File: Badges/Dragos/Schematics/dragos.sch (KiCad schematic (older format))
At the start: 31 parts, among them J1 Conn_01x02, J2 Left, J3 Right, J4 Conn_01x02, J5 Prog, J7 USB_C_Receptacle, SW1 SW_DIP_x01, SW2 Prog, SW3 Power, U1 STM32F042F6Px, U2 TLV1117-33, U3 HX4056, Y1 8MHz

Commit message: Progress on Dragos badge
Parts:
- removed J1, J4: Conn_01x02, Connector_PinHeader_2.54mm:PinHeader_1x02_P2.54mm_Vertical, symbol badge-rescue:Conn_01x02
- removed J2: Left, Connector_PinHeader_2.54mm:PinHeader_1x05_P2.54mm_Vertical, symbol Connector_Generic:Conn_01x05
- removed J3: Right, Connector_PinHeader_2.54mm:PinHeader_1x06_P2.54mm_Vertical, symbol Connector_Generic:Conn_01x06
- removed J5: Prog, Connector_PinHeader_2.54mm:PinHeader_1x04_P2.54mm_Vertical, symbol badge-rescue:Conn_01x04
- removed R4: 0ohm, Resistors_SMD:R_0805_HandSoldering, symbol badge-rescue:R
- removed SW2: Prog, BreadBoardPwr:SK-3296S_switch, symbol Switch:SW_SPDT
- removed U1: STM32F042F6Px, Package_SO:TSSOP-20_4.4x6.5mm_P0.65mm, symbol MCU_ST_STM32F0:STM32F042F6Px
- removed Y1: 8MHz, Crystal:Crystal_SMD_5032-2Pin_5.0x3.2mm, symbol Device:Crystal_Small
- added C12: 100nF, Capacitor_SMD:C_0805_2012Metric, symbol Device:C_Small
- added C13: 1uF, Capacitor_SMD:C_0805_2012Metric, symbol Device:C_Small
- added C14: 4.7uF, Capacitor_SMD:C_0805_2012Metric, symbol Device:C_Small
- added C15, C16: 10pF, Capacitor_SMD:C_0805_2012Metric, symbol Device:C_Small
- added C17, C18: 2.2pF, Capacitor_SMD:C_0805_2012Metric, symbol Device:C_Small
- added D1, D2: LED, LED_SMD:LED_0603_1608Metric, symbol Device:LED
- added D3: LED_ALT, symbol Device:LED_ALT
- added J1: One, Connector_PinHeader_2.54mm:PinHeader_1x08_P2.54mm_Vertical, symbol Connector_Generic:Conn_01x08
- added J2: Two, Connector_PinHeader_2.54mm:PinHeader_1x11_P2.54mm_Vertical, symbol Connector_Generic:Conn_01x11
- added J3: CC2530-ISP, Connector_PinHeader_2.54mm:PinHeader_2x05_P2.54mm_Vertical, symbol Connector_Generic:Conn_02x05_Odd_Even
- added J4: Three, Connector_PinHeader_2.54mm:PinHeader_1x14_P2.54mm_Vertical, symbol Connector_Generic:Conn_01x14
- added J5: Prog, Connector_PinHeader_2.54mm:PinHeader_1x06_P2.54mm_Vertical, symbol Connector_Generic:Conn_01x06
- added J6: Oled_FFS, Connector_FFC-FPC:TE_1-84953-0_1x10-1MP_P1.0mm_Horizontal, symbol Connector_Generic:Conn_01x11
- added J8: Four, Connector_PinHeader_2.54mm:PinHeader_1x13_P2.54mm_Vertical, symbol Connector_Generic:Conn_01x13
- added J9: BreadboardPwr, Connector_PinHeader_2.54mm:PinHeader_1x02_P2.54mm_Vertical, symbol Connector_Generic:Conn_01x02
- added L1: L_Small, Inductor_SMD:L_0603_1608Metric, symbol Device:L_Small
- added R10, R13, R14, R4, R7, R8: 4k7, Resistor_SMD:R_0805_2012Metric, symbol Device:R_Small
- added R11, R12: 330Ohm, Resistor_SMD:R_0805_2012Metric, symbol Device:R_Small
- added R9: 1k, Resistor_SMD:R_0805_2012Metric, symbol Device:R_Small
- added SW2, SW4: SW_DIP_x01, Dragos:1TS002E-2500-2500-CT-HYP-Button, symbol Switch:SW_DIP_x01
- added U1: STM32F411RETx, Package_QFP:LQFP-64_10x10mm_P0.5mm, symbol MCU_ST_STM32F4:STM32F411RETx
- added U4: EByte-CC2530, RF_Module:E18-MS1-PCB, symbol Dragos:EByte-CC2530
- added U5: K1-5202UA-03(5Way_Switch), Dragos:K1-5202UA-03(5way-switch), symbol Dragos:K1-5202UA-03(5Way_Switch)
- added Y1: 12MHz, Crystal:Crystal_SMD_SeikoEpson_TSX3225-4Pin_3.2x2.5mm, symbol Device:Crystal_GND24
- added Y2: 32.768kHz, Crystal:Crystal_SMD_3215-2Pin_3.2x1.5mm, symbol Device:Crystal_Small
- C1, C2: value 20pF -> 100nF
- C4: value 4.7uF -> 100nF
- C6: value 1uF -> 4.7uF
- C7: value 10nF -> 100nF
- R3: value 10k -> 100k
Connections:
- net labels added: Boot0, PA11, PA12, PA13, PA14, PA15, PA8, PB0, PB10, PB12, PB13, PB14, PB15, PB2, PB3, PB4, PB5, PB6, PB7, PB8, PB9, PC0, PC1, PC10, PC11, PC12, PC13, PC2, PC3, PC4, PC5, PC6, PC7, PC8, PC9, PD2
- net labels removed: BOOT0, PF0, PF1, Stat1, Stat2
- wire segments 73 -> 152
- no-connect marks 11 -> 32
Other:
- note added: "Battery Charger IC\n"
- note added: "Boot1"
- note added: "Eye Light, Reverse mount LED"
- note added: "Filter Caps\n"
- note added: "I2C Pullups"
- note added: "Voltage Regulation"
- moved on the sheet: BT1, C10, C11, C8, C9, J7, R1, R2, R5, R6, SW3, U2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

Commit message: Almost done
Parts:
- removed J6: Oled_FFS, Connector_FFC-FPC:TE_1-84953-0_1x10-1MP_P1.0mm_Horizontal, symbol Connector_Generic:Conn_01x11
- removed R10, R4, R7, R8: 4k7, Resistor_SMD:R_0805_2012Metric, symbol Device:R_Small
- removed R2: 10k, Resistor_SMD:R_0805_2012Metric, symbol Device:R_Small
- added C19, C22: 100nF, Capacitor_SMD:C_0805_2012Metric, symbol Device:C_Small
- added C20: 4.7uF, Capacitor_SMD:C_0805_2012Metric, symbol Device:C_Small
- added C21: 4.7uF, Capacitor_SMD:C_2010_5025Metric_Pad1.52x2.65mm_HandSolder, symbol Device:CP_Small
- added C23: 10uF, Capacitor_SMD:C_0805_2012Metric, symbol Device:C_Small
- added RN1: 10k, Resistor_SMD:R_Array_Concave_2x0603, symbol Device:R_Pack02
- added RN2: 4k7, Resistor_SMD:R_Array_Concave_4x0603, symbol Device:R_Pack04
- added U6: Formike-OLED, symbol Dragos:Formike-OLED
- D3: footprint (none) -> Dragos:T776-ReverseMountLED
- Power->1: renamed from SW3; value Power -> SW3
- R1: value 10k -> 760k
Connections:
- net PA8: now also RN2.8 (R1.2)
- net PB6: now also RN2.6 (R3.2), U6.18 (D0)
- net PB7: now also RN2.5 (R4.2), U6.19 (D1), U6.20 (D2)
- net PB8: now also RN2.7 (R2.2)
- net PB9: now also U6.14 (RES#)
- net VCC: now also C19.2, C20.2, C22.1, C23.1, RN2.1 (R1.1), RN2.2 (R2.1), RN2.3 (R3.1), RN2.4 (R4.1), U6.11 (BS1), U6.28 (VCC), U6.6 (VBAT), U6.9 (VDD)
- net VSS: now also C19.1, C20.1, RN1.3 (R2.2), RN1.4 (R1.2), U6.1 (GND), U6.10 (BS0), U6.12 (BS2), U6.16 (R/W), U6.17 (E/RD), U6.21 (D3), U6.22 (D4), U6.23 (D5), U6.24 (D6), U6.25 (D7), U6.30 (GND), U6.8 (VSS); no longer R1.1
- net at J7.A5 (CC1): now also RN1.1 (R1.1); no longer R1.2
- net at J7.B5 (CC2): now also RN1.2 (R2.1)
- new net: R1.1, U6.26 (IREF)
- new net: C21.1, U6.27 (VCOMH)
- new net: C21.2, C22.2, C23.2, R1.2, U6.29 (VLSS)
- no-connect marks 32 -> 27

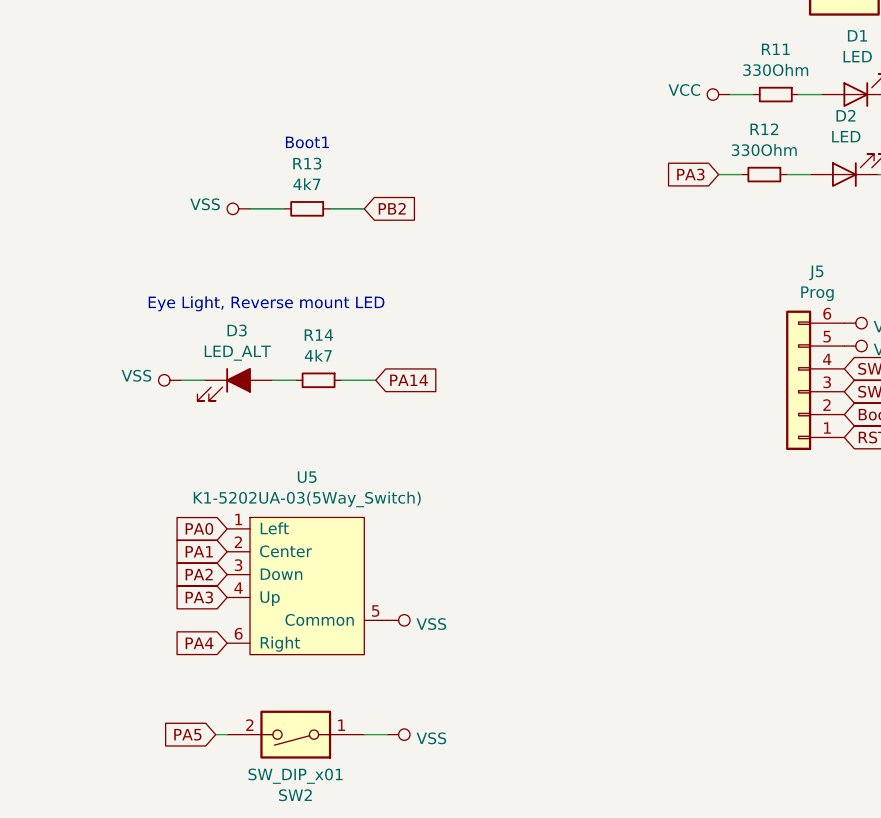
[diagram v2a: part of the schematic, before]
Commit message: Added bom
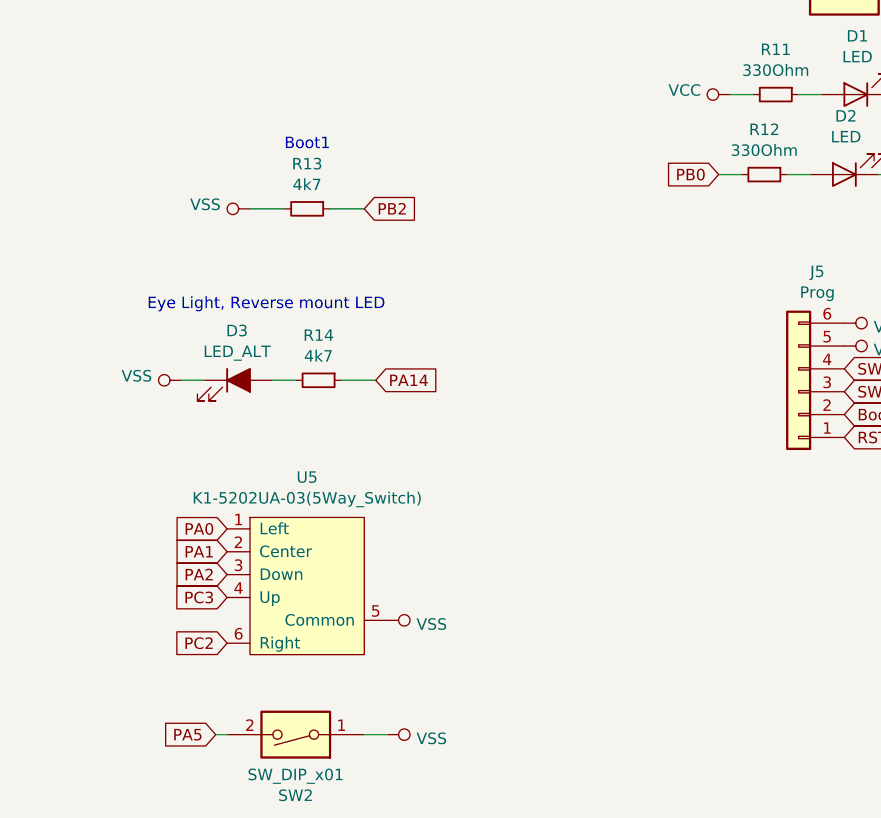
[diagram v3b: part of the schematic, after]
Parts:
- J3: footprint Connector_PinHeader_2.54mm:PinHeader_2x05_P2.54mm_Vertical -> Connector_PinHeader_1.00mm:PinHeader_2x05_P1.00mm_Vertical
- J5: footprint Connector_PinHeader_2.54mm:PinHeader_1x06_P2.54mm_Vertical -> Connector_PinHeader_1.00mm:PinHeader_1x06_P1.00mm_Vertical
- U6: footprint (none) -> Connector_FFC-FPC:Hirose_FH12-30S-0.5SH_1x30-1MP_P0.50mm_Horizontal
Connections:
- net PA3: no longer R12.2, U5.4 (Up)
- net PA4: no longer U5.6 (Right)
- net PB0: now also R12.2
- net PC2: now also U5.6 (Right)
- net PC3: now also U5.4 (Up)
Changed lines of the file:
@@
 F 0 "J3" H 14300 7817 50  0000 C CNN
 F 1 "CC2530-ISP" H 14300 7726 50  0000 C CNN
-F 2 "Connector_PinHeader_2.54mm:PinHeader_2x05_P2.54mm_Vertical" H 14250 7400 50  0001 C CNN
+F 2 "Connector_PinHeader_1.00mm:PinHeader_2x05_P1.00mm_Vertical" H 14250 7400 50  0001 C CNN
 F 3 "~" H 14250 7400 50  0001 C CNN
 	1    14250 7400
@@
 F 0 "J5" H 8518 4275 50  0000 C CNN
 F 1 "Prog" H 8518 4366 50  0000 C CNN
-F 2 "Connector_PinHeader_2.54mm:PinHeader_1x06_P2.54mm_Vertical" H 8600 4800 50  0001 C CNN
+F 2 "Connector_PinHeader_1.00mm:PinHeader_1x06_P1.00mm_Vertical" H 8600 4800 50  0001 C CNN
 F 3 "~" H 8600 4800 50  0001 C CNN
 	1    8600 4800
@@
 Wire Wire Line
 	8250 3850 8350 3850
-Text GLabel 8250 3850 0    50   Input ~ 0
-PA3
 $Comp
 L Connector_Generic:Conn_01x02 J9
@@
 PA2
 Text GLabel 6100 5700 0    50   Input ~ 0
-PA3
+PC3
 Text GLabel 6100 5900 0    50   Input ~ 0
-PA4
+PC2
 $Comp
 L power:VSS #PWR0146
@@
 F 0 "U6" H 3333 8115 50  0000 C CNN
 F 1 "Formike-OLED" H 3333 8024 50  0000 C CNN
-F 2 "" H 3550 7250 50  0001 C CNN
+F 2 "Connector_FFC-FPC:Hirose_FH12-30S-0.5SH_1x30-1MP_P0.50mm_Horizontal" H 3550 7250 50  0001 C CNN
 F 3 "" H 3550 7250 50  0001 C CNN
 	1    3250 6400
@@
 Text GLabel 3550 6250 2    50   Input ~ 0
 PB9
+Text GLabel 8250 3850 0    50   Input ~ 0
+PB0
 $EndSCHEMATC
